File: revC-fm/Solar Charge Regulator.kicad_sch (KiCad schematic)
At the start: 25 parts, among them U22 ‎LT3652HVEMSE#TRPBF‎

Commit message: working revC
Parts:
- added R23: 0, Resistor_SMD:R_0603_1608Metric, symbol Device:R_US
- C79: renamed from C85; footprint Capacitor_Tantalum_SMD:CP_EIA-7132-28_AVX-C -> Capacitor_Tantalum_SMD:CP_EIA-7343-20_Kemet-V
- renumbered C78 to C73, C79 to C74, C80 to C75, C81 to C76, C83 to C77, C84 to C78, C82 to C80, D8 to D10, D7 to D11, D6 to D9, R163 to R137, R161 to R138, R165 to R139, R162 to R140, R164 to R142, R166 to R143, R158 to R144, R160 to R145, R159 to R146, U22 to U19
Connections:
- net BATT_NTC: now also R23.2; no longer U19.8 (NTC)
- new net: R23.1, U19.8 (NTC)
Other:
- moved on the sheet: C77, C78, C79, R139, R142, R143

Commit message: working revC
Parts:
- removed R23: 1k, Resistor_SMD:R_0603_1608Metric, symbol Device:R_US
- added R80: 0, Resistor_SMD:R_1210_3225Metric, symbol Device:R_US
- added R83, R86: 0, Resistor_SMD:R_0603_1608Metric, symbol Device:R_US
- D7: renamed from D11; symbol mainboard-rescue:D-Device-mainboard-rescue -> Device:D
- L4: renamed from L5; footprint mainboard-SLI:SRN6045TA-330M -> SierraLobo:SRN6045TA-330M
- R91: renamed from R146; value 1Meg -> 100k
- R92: renamed from R145; value 1Meg -> 100k
- U17: renamed from U19; footprint mainboard-SLI:MSOP-12-1EP_3x4mm_P0.65mm_EP1.65x2.85mm_ThermalVias -> Package_SO:MSOP-12-1EP_3x4mm_P0.65mm_EP1.65x2.85mm_ThermalVias; symbol mainboard_SLI:LTC3652HV -> SierraLobo:LTC3652HV
- renumbered C73 to C51, C74 to C52, C75 to C53, C76 to C54, C77 to C55, C78 to C56, C79 to C57, C80 to C58, D9 to D5, D10 to D6, R137 to R81, R138 to R82, R140 to R84, R139 to R87, R142 to R88, R143 to R89, R144 to R90, TH2 to TH1
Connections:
- net VCHRG: now also R83.1; no longer R87.1
- net VSOLAR: now also R80.1
- net ~{CHRG}: now also U17.4 (~{CHG})
- net at C51.1, C52.1, C53.1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: now also R80.2
- new net: R83.2, R86.1, R87.1
- new net VBATT: R86.2
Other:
- moved on the sheet: D5, R82, R84, R87, R91

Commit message: routing fm
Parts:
- removed R23: 1k, Resistor_SMD:R_0603_1608Metric, symbol Device:R_US
- removed R83, R86: 0, Resistor_SMD:R_0603_1608Metric, symbol Device:R_US
- removed TH1: 10k, Resistor_SMD:R_0603_1608Metric, symbol Device:Thermistor_NTC_US
- added D17: YEL, LED_SMD:LED_0603_1608Metric, symbol Device:LED
- added Q1: ~, Package_TO_SOT_SMD:SOT-323_SC-70, symbol Device:Q_PNP_BEC
- added Q34: MMDT3946, Package_TO_SOT_SMD:SOT-363_SC-70-6, symbol Transistor_BJT:MMDT3946
- added R228, R23, R39: 1Meg, Resistor_SMD:R_0603_1608Metric, symbol Device:R_US
- added R23: 1k, Resistor_SMD:R_0603_1608Metric, symbol Device:R_US
- C55, C56: footprint Capacitor_SMD:C_1210_3225Metric -> Capacitor_SMD:C_1206_3216Metric
- R82: value 267k -> 523k
- R84: value 51k -> 100k
- R91: value 100k -> 10k
- R92: value 100k -> 2.7k
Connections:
- net GND: now also D17.1 (K), Q34.1 (E1)
- net VCHRG: now also R87.1
- net ~{CHRG}: now also R91.1, R39.1; no longer R91.2
- net at C51.1, C52.1, C53.1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: now also R228.1
- net at U17.3 (~{SHDN}): now also R23.1
- removed net 3.3V: R90.1, R91.1, R92.1
- net SLR_CHRG_NTC renamed CHRG
- net VSOLAR renamed VIN
- net ~{CHRG_SHDN}: no longer names the net of R92.2
- net ~{CHRG_SHDN}: now also D17.2 (A)
- new net: Q34.5 (B2), R39.2
- new net: Q34.2 (B1), R23.1
- new net: Q1.3 (C), R92.1
- new net: Q1.1 (B), R91.2
- new net: Q34.3 (C2), R90.1
- new net LED_PWR: Q1.2 (E)
- new net SHDN: R23.2
- new net VIO: Q34.4 (E2)
- new net ~{SHDN}: Q34.6 (C1), R228.2, R23.2
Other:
- added sheet Temp Sensor 1 (temp_senkicad_sch.kicad_sch)
- note added: "INPUT: Solar Panel Voltage 6.5-34V Inputs lower than 6.5V can be obtained if Vfloat is < 5.5V Adjust R161&162 for vpp programming"
- note added: "Input: 2x3U Pumpkin Cells in parallel (7 series cells) Vdc = 17.5V cell BOL Vpp = 2.405V BOL Vpp = 16.835V p15 datasheet: RIN1/RIN2 = (VIN(MIN)/2.7) - 1 RIN1/RIN2 = (16.825/2.7)-1 = 5.23 RIN1 = 267k VINMIN actual = XXX"
- note added: "May need to remove NTC input as this charger will stop charging at at certain temps."
- note added: "OUTPUT: 8.4Vfloat, 1.4A. 12W adjust feedback divider for lower/higher float voltage."
- note added: "place @ MCU"
- note added: "place close to inductor or IC"
- note removed: "INPUT: Solar Panels 9-34V Lower input of 6.5V can be adjusted if Vfloat is < 5.5V Adjust R161&162 for vpp programming"
- note removed: "Input: 2x3U Pumpkin Cells in parallel (7 series cells) Vdc = 17.5V cell BOL Vpp = 2.405V BOL Vpp = 16.835V RIN1/RIN2 = (16.825/2.7)-1 = 5.23 RIN1 = 267k VINMIN actual = XXX"
- note removed: "OUTPUT: 8.4Vfloat, 1.4A. 12W adjust feedback divider for lower/higher float voltage. Vfloat must be >= Vin+1 due to buck topology"
- note removed: "Vsolar in 6.5 - 40V Vin >= Vout+1 as this is a buck converter"
- moved on the sheet: C51, C52, C53, C54, C55, C56, C57, C58, D5, D6, D7, L4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

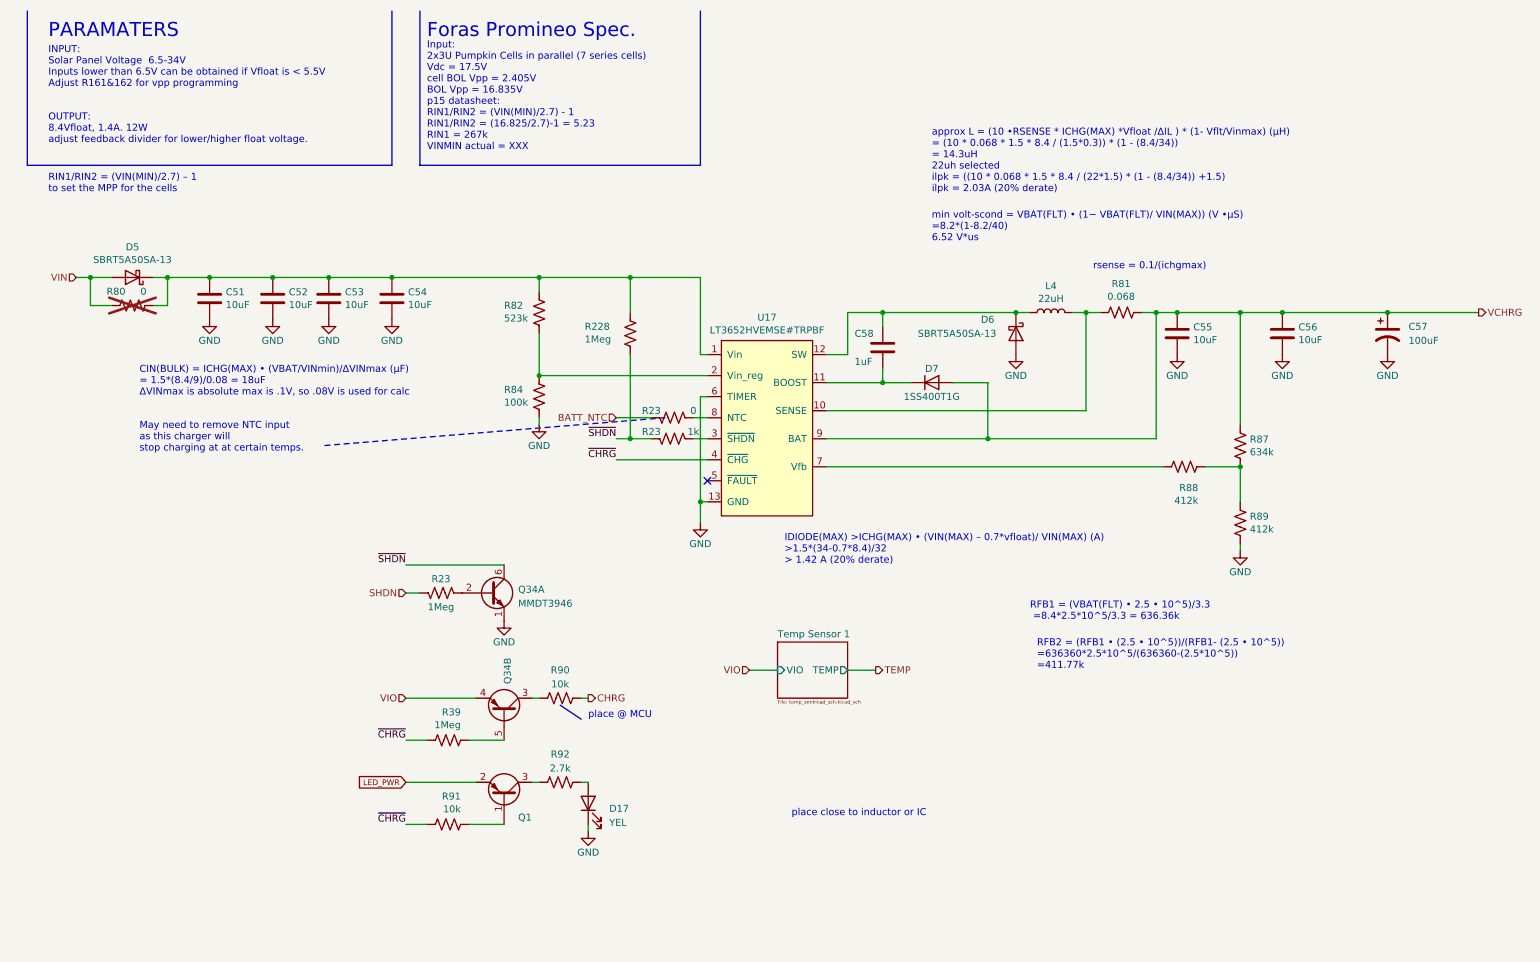
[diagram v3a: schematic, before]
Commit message: updated analog , solar comp, layout
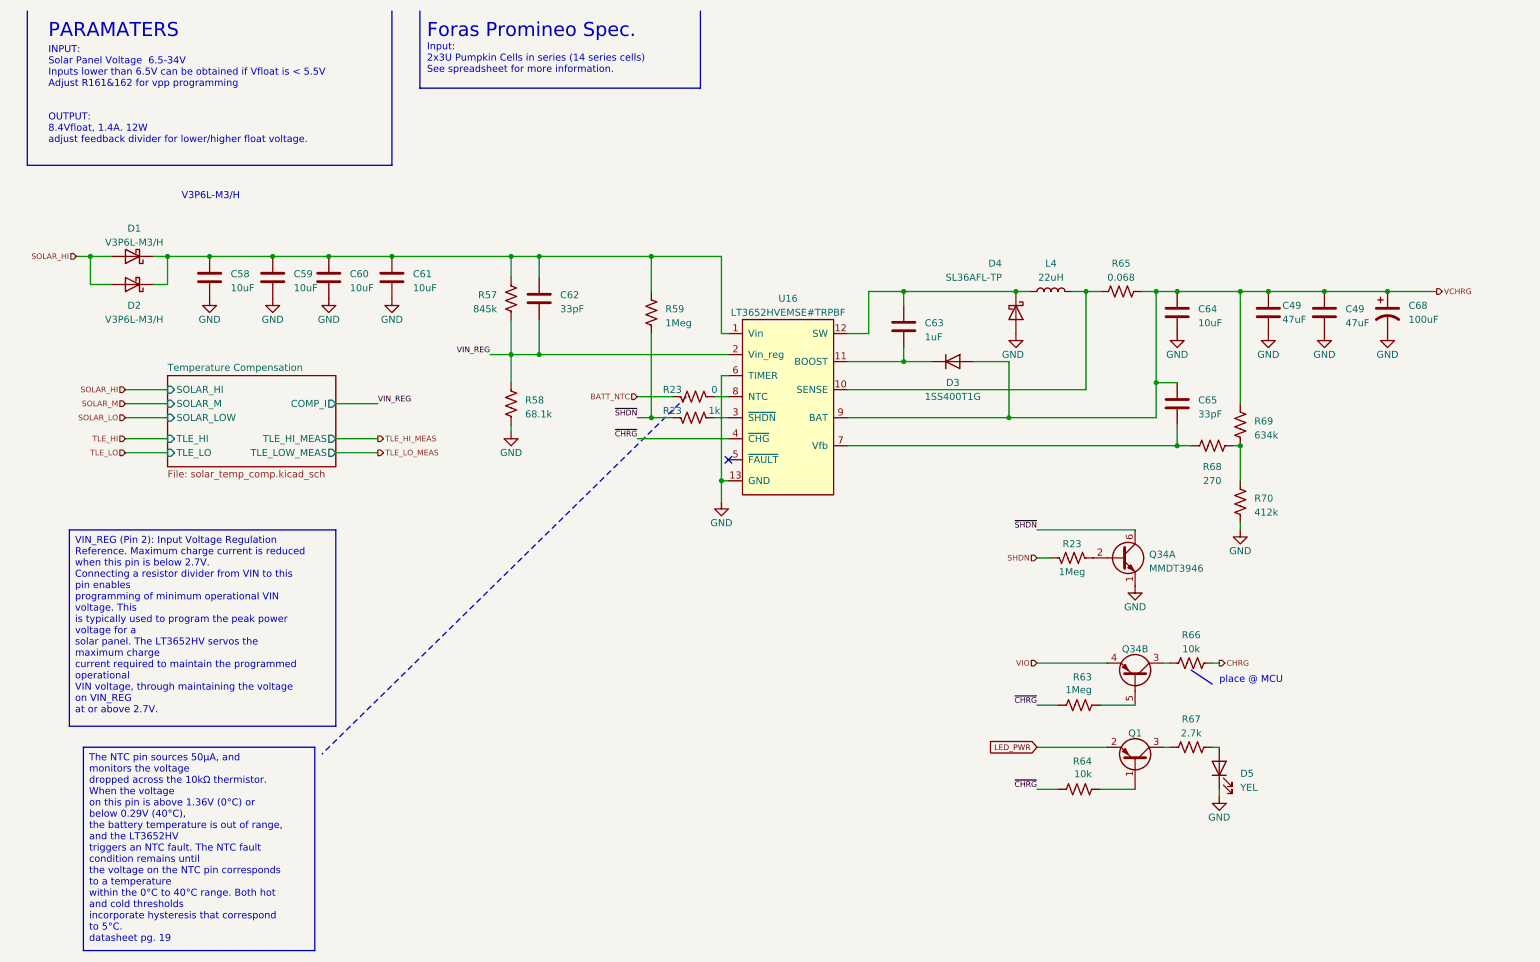
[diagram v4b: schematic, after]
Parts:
- removed C56: 10uF, Capacitor_SMD:C_1206_3216Metric, symbol Device:C
- removed R80: 0, Resistor_SMD:R_1210_3225Metric, symbol Device:R_US
- added C49 (x2): 47uF, Capacitor_SMD:C_1206_3216Metric, symbol Device:C
- added C62, C65: 33pF, Capacitor_SMD:C_0603_1608Metric, symbol Device:C
- added D2: V3P6L-M3/H, SierraLobo:SMP, symbol mainboard-rescue:D_Schottky-Device-mainboard-rescue
- D1: renamed from D5; value SBRT5A50SA-13 -> V3P6L-M3/H; footprint Diode_SMD:D_SMA -> SierraLobo:SMP
- D4: renamed from D6; value SBRT5A50SA-13 -> SL36AFL-TP
- L4: footprint SierraLobo:SRN6045TA-330M -> Inductor_SMD:L_Coilcraft_XAL6060-XXX
- R57: renamed from R82; value 523k -> 845k
- R58: renamed from R84; value 100k -> 68.1k
- R68: renamed from R88; value 412k -> 270
- renumbered C51 to C58, C52 to C59, C53 to C60, C54 to C61, C58 to C63, C55 to C64, C57 to C68, D7 to D3, D17 to D5, R228 to R59, R39 to R63, R91 to R64, R81 to R65, R90 to R66, R92 to R67, R87 to R69, R89 to R70, U17 to U16
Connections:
- net GND: now also C49.2, C49.2
- net VCHRG: now also C49.1, C49.1, C65.1
- net at C58.1, C59.1, C60.1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: now also C62.1, D2.1 (K)
- net VIN_REG: now reaches R57.2, R58.1, U16.2 (Vin_reg)
- net VIN_REG: now also C62.2
- net at R68.1, U16.7 (Vfb): now also C65.2
- net VIN renamed SOLAR_HI
- net SOLAR_HI: now also D2.2 (A)
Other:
- removed sheet Temp Sensor 1
- added sheet Temperature Compensation (solar_temp_comp.kicad_sch)
- note added: "Input: 2x3U Pumpkin Cells in series (14 series cells) See spreadsheet for more information."
- note added: "V3P6L-M3/H"
- note removed: "CIN(BULK) = ICHG(MAX) • (VBAT/VINmin)/ΔVINmax (µF) = 1.5*(8.4/9)/0.08 = 18uF ΔVINmax is absolute max is .1V, so .08V is used for calc"
- note removed: "IDIODE(MAX) >ICHG(MAX) • (VIN(MAX) – 0.7*vfloat)/ VIN(MAX) (A) >1.5*(34-0.7*8.4)/32 > 1.42 A (20% derate)"
- note removed: "Input: 2x3U Pumpkin Cells in parallel (7 series cells) Vdc = 17.5V cell BOL Vpp = 2.405V BOL Vpp = 16.835V p15 datasheet: RIN1/RIN2 = (VIN(MIN)/2.7) - 1 RIN1/RIN2 = (16.825/2.7)-1 = 5.23 RIN1 = 267k VINMIN actual = XXX"
- note removed: "May need to remove NTC input as this charger will stop charging at at certain temps."
- note removed: "RFB1 = (VBAT(FLT) • 2.5 • 10^5)/3.3 =8.4*2.5*10^5/3.3 = 636.36k"
- note removed: "RFB2 = (RFB1 • (2.5 • 10^5))/(RFB1- (2.5 • 10^5)) =636360*2.5*10^5/(636360-(2.5*10^5)) =411.77k"
- note removed: "RIN1/RIN2 = (VIN(MIN)/2.7) – 1 to set the MPP for the cells"
- note removed: "approx L = (10 •RSENSE * ICHG(MAX) *Vfloat /ΔIL ) * (1- Vflt/Vinmax) (µH) = (10 * 0.068 * 1.5 * 8.4 / (1.5*0.3)) * (1 - (8.4/34)) = 14.3uH 22uh selected ilpk = ((10 * 0.068 * 1.5 * 8.4 / (22*1.5) * (1 - (8.4/34)) +1.5) ilpk = 2.03A (20% derate)"
- note removed: "min volt-scond = VBAT(FLT) • (1− VBAT(FLT)/ VIN(MAX)) (V •µS) =8.2*(1-8.2/40) 6.52 V*us"
- note removed: "place close to inductor or IC"
- note removed: "rsense = 0.1/(ichgmax)"
- moved on the sheet: C58, C59, C60, C61, C63, C64, C68, D1, D3, D4, D5, L4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

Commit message: routing
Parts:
- renumbered C58 to C61, C59 to C62, C60 to C63, C61 to C64, C62 to C65, C64 to C66, C68 to C69, C63 to C70, C65 to C71, D4 to D3, D3 to D4, R65 to R52, R57 to R53, R59 to R54, R58 to R56, R69 to R58, R68 to R59, R70 to R60, R66 to R62, R67 to R64, R64 to R65, U16 to U18

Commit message: changed RF connector to TH
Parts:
- renumbered C61 to C60, C62 to C61, C63 to C62, C64 to C63, C65 to C64, C66 to C65, C69 to C68, C70 to C69, C71 to C70, R52 to R54, R53 to R55, R54 to R56, R56 to R58, R58 to R60, R59 to R61, R60 to R62, R62 to R64, R63 to R65, R64 to R66, R65 to R67, U18 to U17

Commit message: working revC review changes
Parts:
- renumbered C60 to C61, C61 to C62, C62 to C63, C63 to C64, C64 to C65, C65 to C66, C68 to C69, C69 to C70, C70 to C71, D5 to LED7, R54 to R60, R55 to R61, R56 to R62, R58 to R64, R60 to R66, R61 to R67, R62 to R68, R64 to R70, R65 to R71, R66 to R72, R67 to R73, U17 to U18
